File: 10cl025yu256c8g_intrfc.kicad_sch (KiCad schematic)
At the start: 82 parts, among them Q1 AO3400A, Q2 AO3400A, Q3 AO3400A, Q4 AO3400A, Q5 AO3400A, Q6 AO3400A, SW10 SW_DIP_x01, SW11 SW_DIP_x01, SW12 SW_DIP_x01, SW13 FPGA_PB1, SW14 FPGA_PB2, SW15 FPGA_PB3, SW16 FPGA_PB4, SW17 FPGA_PB5, SW3 SW_DIP_x01, SW4 SW_DIP_x01, SW5 SW_DIP_x01, SW6 SW_DIP_x01, SW7 SW_DIP_x01, SW8 SW_DIP_x01, SW9 SW_DIP_x01, U10 SC39-11GWA, U5 SC39-11GWA, U6 SC39-11GWA, U7 SC39-11GWA, U8 SC39-11GWA, U9 SC39-11GWA

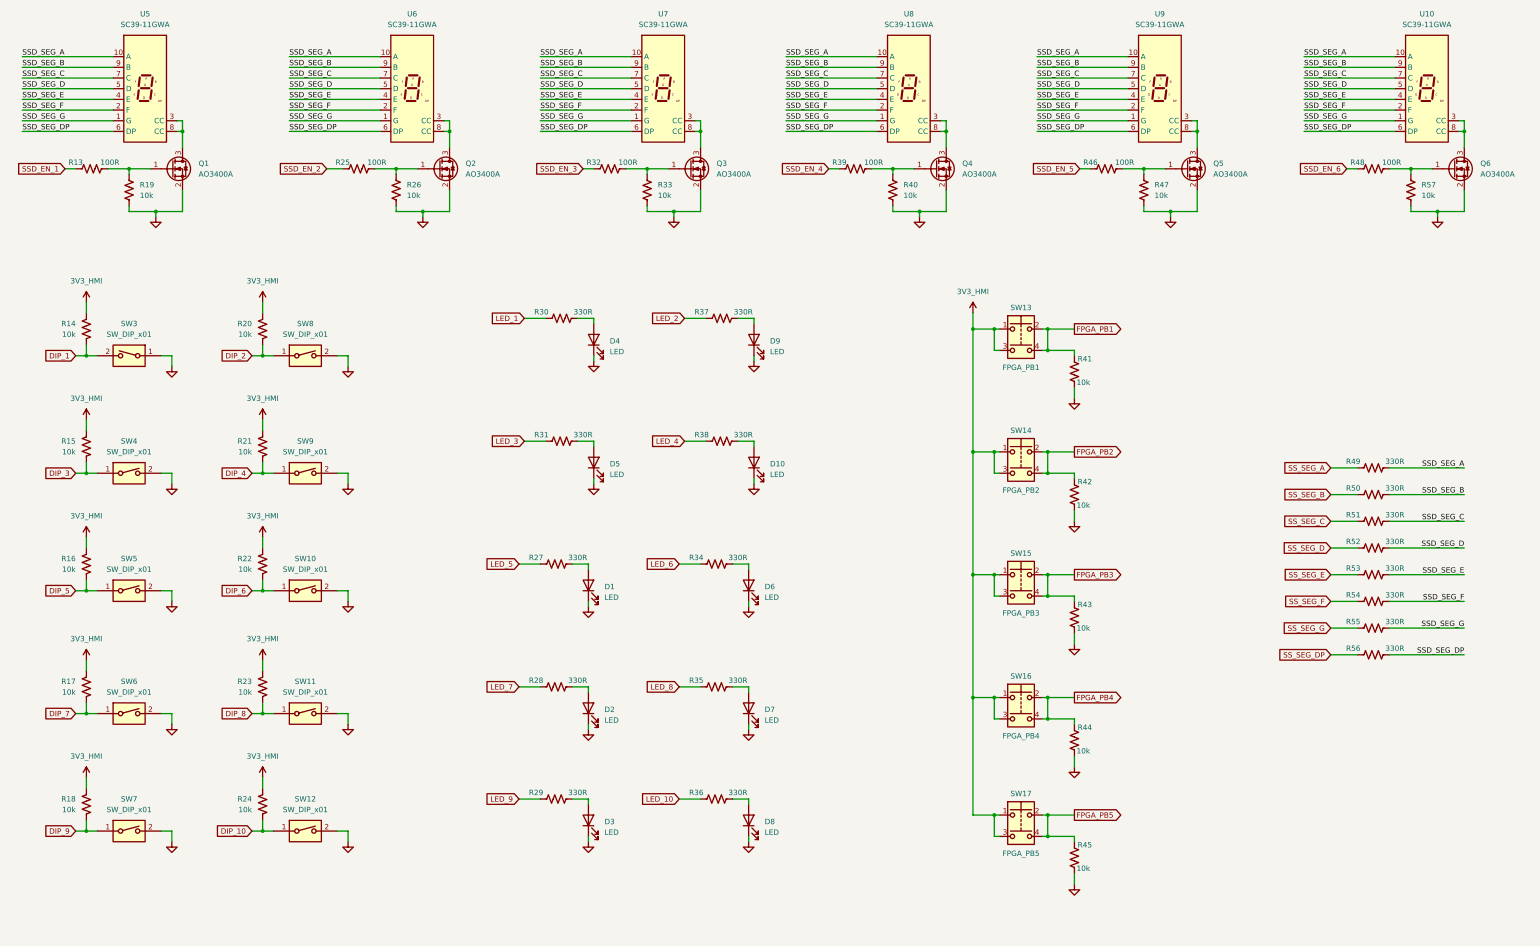
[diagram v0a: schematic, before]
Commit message: Decoupling done
The decoupling for the 10CL025 was completed using the evaluation module as reference.
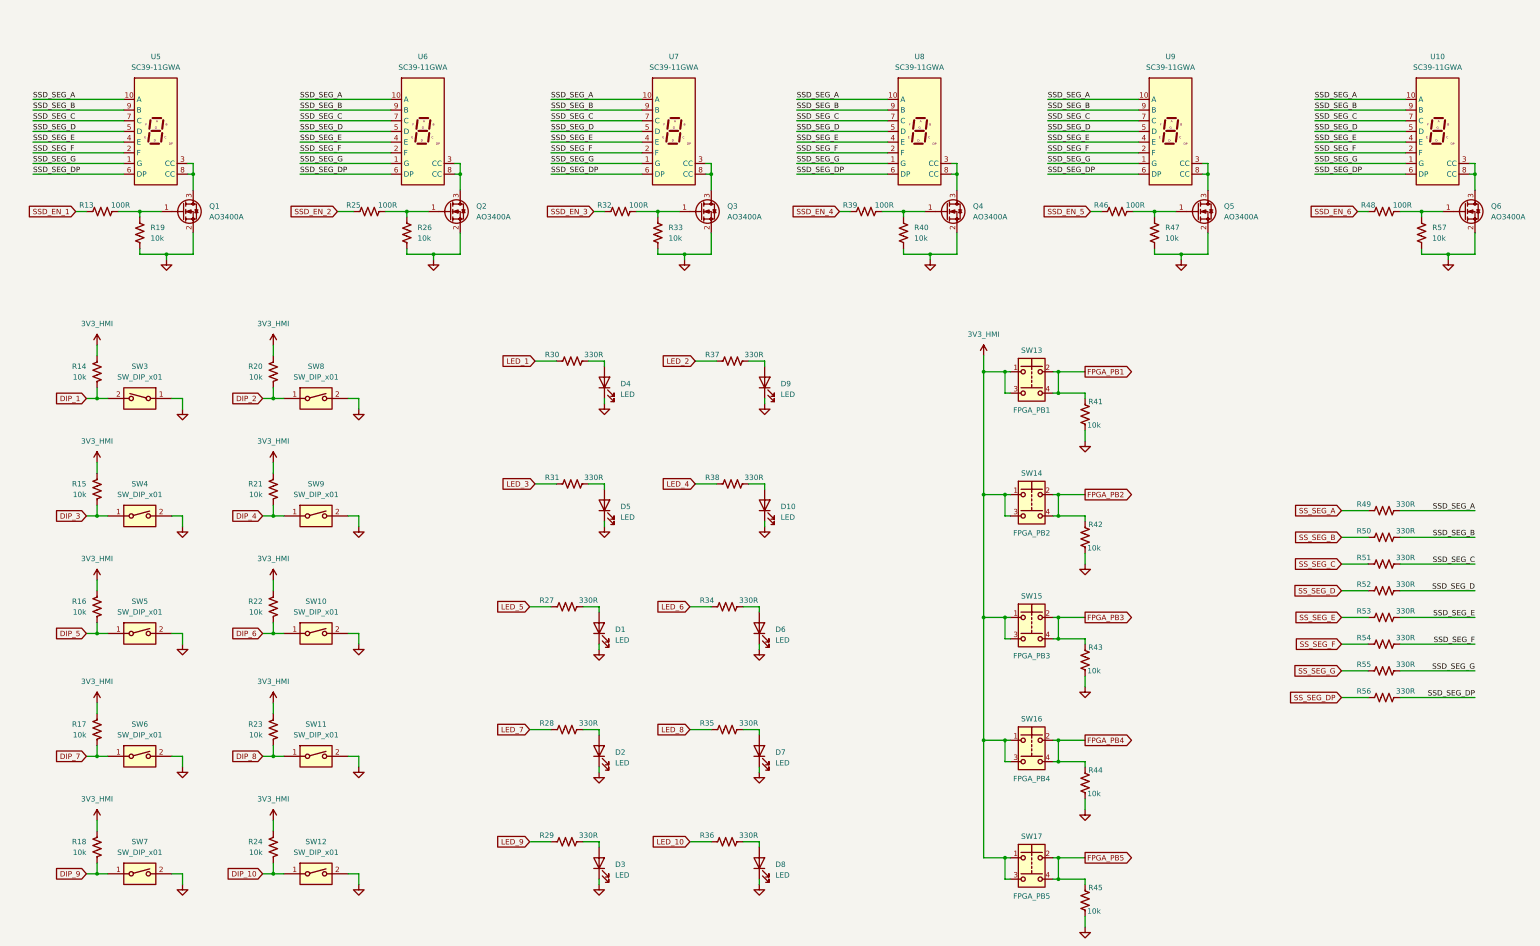
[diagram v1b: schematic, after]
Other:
- moved on the sheet: D1, D10, D2, D3, D4, D5, D6, D7, D8, D9, Q1, Q2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

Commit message: No big changes made from last time
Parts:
- R27, R28, R30, R31, R34, R35, R36, R37, R38, R49, R50, R51, R52, R53, R54, R55, R56: value 330R -> 1.5K
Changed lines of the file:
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@@
 			)
 		)
-		(property "Value" "330R"
+		(property "Value" "1.5K"
 			(at 358.14 161.036 90)
 			(show_name no)
@@
 			)
 		)
-		(property "Value" "330R"
+		(property "Value" "1.5K"
 			(at 203.2 135.636 90)
 			(show_name no)
@@
 			)
 		)
-		(property "Value" "330R"
+		(property "Value" "1.5K"
 			(at 165.1 135.636 90)
 			(show_name no)
@@
 			)
 		)
-		(property "Value" "330R"
+		(property "Value" "1.5K"
 			(at 163.83 194.056 90)
 			(show_name no)
@@
 			)
 		)
-		(property "Value" "330R"
+		(property "Value" "1.5K"
 			(at 358.14 154.686 90)
 			(show_name no)
@@
 			)
 		)
-		(property "Value" "330R"
+		(property "Value" "1.5K"
 			(at 163.83 164.846 90)
 			(show_name no)
@@
 			)
 		)
-		(property "Value" "330R"
+		(property "Value" "1.5K"
 			(at 358.14 173.736 90)
 			(show_name no)
@@
 			)
 		)
-		(property "Value" "330R"
+		(property "Value" "1.5K"
 			(at 358.14 167.386 90)
 			(show_name no)
@@
 			)
 		)
-		(property "Value" "330R"
+		(property "Value" "1.5K"
 			(at 201.93 164.846 90)
 			(show_name no)
@@
 			)
 		)
-		(property "Value" "330R"
+		(property "Value" "1.5K"
 			(at 358.14 141.986 90)
 			(show_name no)
@@
 			)
 		)
-		(property "Value" "330R"
+		(property "Value" "1.5K"
 			(at 358.14 186.436 90)
 			(show_name no)
@@
 			)
 		)
-		(property "Value" "330R"
+		(property "Value" "1.5K"
 			(at 201.93 194.056 90)
 			(show_name no)
@@
 			)
 		)
-		(property "Value" "330R"
+		(property "Value" "1.5K"
 			(at 165.1 106.426 90)
 			(show_name no)
@@
 			)
 		)
-		(property "Value" "330R"
+		(property "Value" "1.5K"
 			(at 358.14 180.086 90)
 			(show_name no)
@@
 			)
 		)
-		(property "Value" "330R"
+		(property "Value" "1.5K"
 			(at 358.14 148.336 90)
 			(show_name no)
@@
 			)
 		)
-		(property "Value" "330R"
+		(property "Value" "1.5K"
 			(at 201.93 220.726 90)
 			(show_name no)
@@
 			)
 		)
-		(property "Value" "330R"
+		(property "Value" "1.5K"
 			(at 203.2 106.426 90)
 			(show_name no)
